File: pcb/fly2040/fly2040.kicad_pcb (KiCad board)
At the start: 4 copper layers, 23 x 18 mm, 47 parts, among them J1 Conn_01x02, J10 Conn_01x02, J2 Conn_01x02, J3 Conn_01x02, J4 Conn_01x02, J5 Conn_01x02, J6 Conn_01x02, J7 Conn_01x02, J8 Conn_01x06, J9 Conn_01x02, SW1 EVPAWED40, U1 RP2040, U2 W25Q16JVUXIQ, U3 RS0102YH8, U4 TPS613222ADBVR, X1 SMD-3225_4P_12.000MHZ_9PF

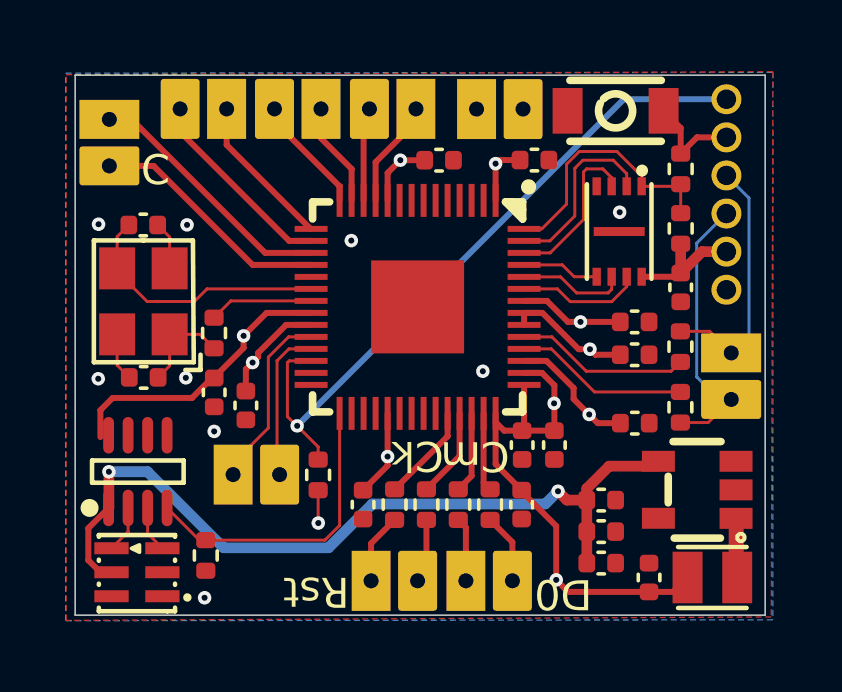
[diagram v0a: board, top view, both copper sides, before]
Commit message: Added more outputs. Improved board layout for panel. Added panel files
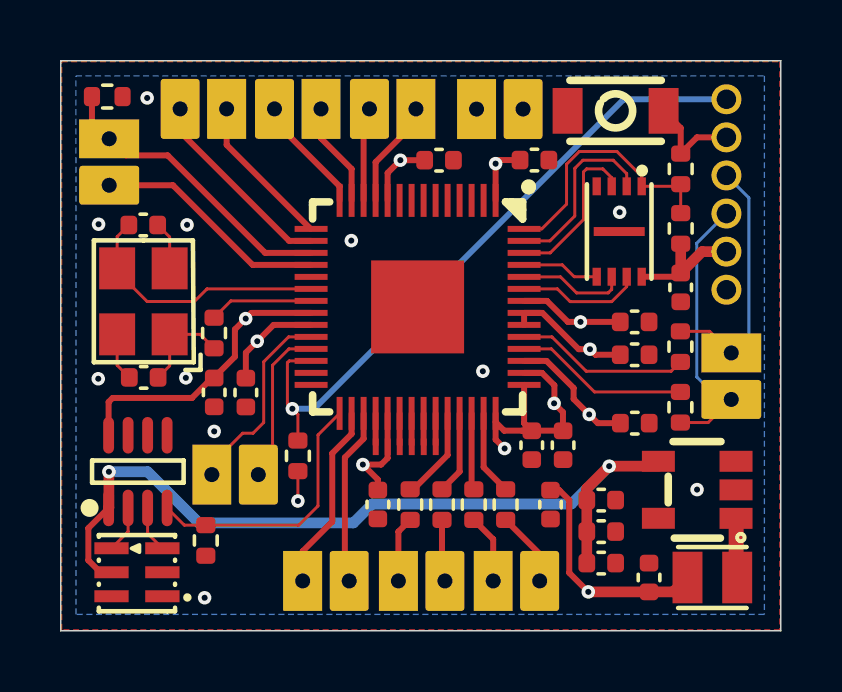
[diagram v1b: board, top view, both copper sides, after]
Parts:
- added J11: Conn_01x02, kicad_lceda:TH_Pads_1x02_P1.50mml, F.Cu at (78.5, 66.7)
- added J12: Conn_01x06, kicad_lceda:Pad_6Pin, F.Cu at (81.9, 64.1)
- added R12: 10k, Resistor_SMD:R_0402_1005Metric, F.Cu at (72.0, 50.6)
- moved C8 0.96 mm to (86.7, 64.2)
- moved R2 0.93 mm to (78.3, 62.6)
- moved J3 0.91 mm to (81.7, 66.7)
- moved J4 0.91 mm to (84.8, 66.7)
- moved J7 0.71 mm to (75.4, 63.2)
- moved J2 0.65 mm to (72.0, 52.0)
- moved R10 0.52 mm to (84.2, 64.2)
- moved R11 0.52 mm to (85.2, 64.2)
- moved R8 0.52 mm to (82.0, 64.2)
- moved R9 0.52 mm to (83.1, 64.2)
- moved R7 0.50 mm to (75.2, 65.4)
- moved C7 0.49 mm to (81.0, 64.2)
- moved C4 0.43 mm to (76.6, 60.5)
- moved C9 0.32 mm to (86.1, 62.2)
- moved C6 0.29 mm to (87.1, 62.2)
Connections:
- net NS_14 renamed NS_CPU_PD
- U1 pad 30: unconnected-(U1-GPIO19-Pad30) -> NS_19
- U1 pad 31: unconnected-(U1-GPIO20-Pad31) -> NS_20
- U1 pad 32: unconnected-(U1-GPIO21-Pad32) -> PAD_21
- U1 pad 34: unconnected-(U1-GPIO22-Pad34) -> PAD_22
- U1 pad 35: unconnected-(U1-GPIO23-Pad35) -> PAD_23
- U1 pad 36: unconnected-(U1-GPIO24-Pad36) -> PAD_24
- U1 pad 37: unconnected-(U1-GPIO25-Pad37) -> PAD_25
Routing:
- net NS_19: track 0.00 -> 6.26 mm
- net NS_20: track 0.00 -> 5.90 mm
- net NS_CPU_PD: track 7.82 -> 9.95 mm
- net LED_EN: track 10.1 -> 8.92 mm
- net PAD_25: track 0.00 -> 1.04 mm
- net PAD_24: track 0.00 -> 1.04 mm
- net PAD_23: track 0.00 -> 1.04 mm
- net PAD_22: track 0.00 -> 1.04 mm
- net PAD_21: track 0.00 -> 1.04 mm
- net +3V3: track 43.3 -> 42.3 mm, vias 8 -> 9
- net RST: track 23.3 -> 22.3 mm
- net DBG_CLK: track 5.73 -> 6.60 mm
- net +1V1: track 26.4 -> 25.7 mm
- net GND: vias 9 -> 11
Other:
- board size 23 x 18 mm -> 24 x 19 mm
- board text added: "19"
- board text added: "20"
- board text removed: "C"
- board text removed: "Ck"
- board text removed: "Cm"
- board text removed: "Rst"

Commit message: Added tiny double sided (ds) board.
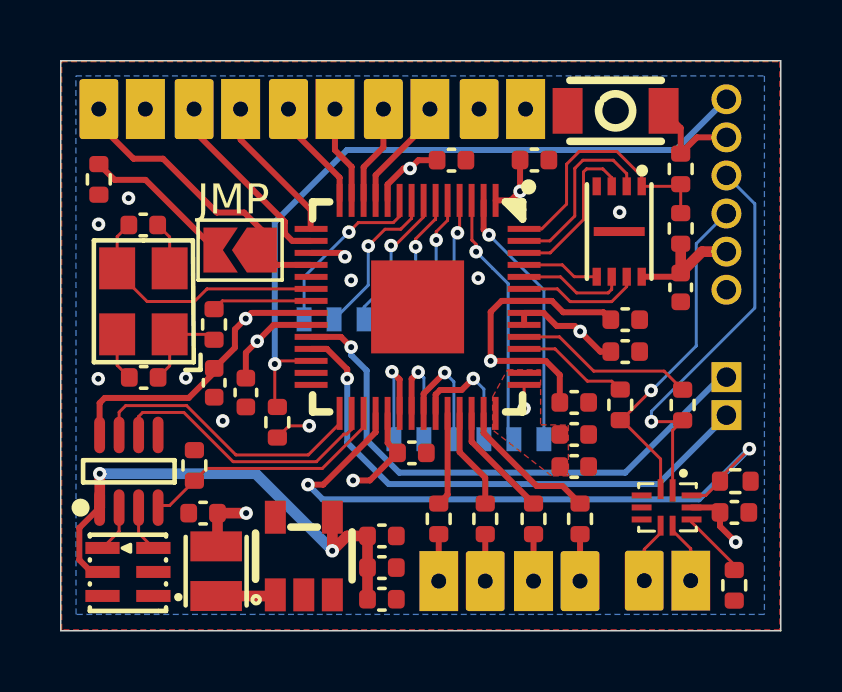
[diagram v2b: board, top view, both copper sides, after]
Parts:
- added JP1: Jumper_2_Open, kicad_lceda:SolderJumper-2_P1.3mm_Open_TrianglePad1.0x1.5mm_Sm, F.Cu at (76.4, 55.7)
- added R13: 10k, Resistor_SMD:R_0402_1005Metric, F.Cu at (92.9, 63.4)
- added R14: 10k, Resistor_SMD:R_0402_1005Metric, F.Cu at (92.8, 66.9)
- added U5: RS2227XUTQK10, kicad_lceda:WQFN-10_L1.8-W1.4-P0.40-BL, F.Cu at (90.6, 64.3)
- J11: value Conn_01x02 -> Conn_01x06; footprint kicad_lceda:TH_Pads_1x02_P1.50mml -> kicad_lceda:Pad_6Pin; moved to B.Cu
- J12: moved to B.Cu
- J7: footprint kicad_lceda:TH_Pads_1x02_P1.50mml -> kicad_lceda:PinHeader_Sm_1x02_P1.27mm_Vertical
- moved J7 17.5 mm to (92.6, 59.9), turned to 0 degrees
- moved L1 16.5 mm to (75.6, 66.4), turned to 90 degrees
- moved C15 15.0 mm to (75.1, 64.5), turned to 180 degrees
- moved U4 13.3 mm to (78.5, 65.9), turned to -90 degrees
- moved J5 7.71 mm to (91.4, 66.7), turned to -90 degrees
- moved C17 7.65 mm to (81.1, 67.3)
- moved C16 7.65 mm to (81.1, 66.3)
- moved C18 7.37 mm to (81.1, 65.2)
- moved J11 6.24 mm to (84.0, 63.9), turned to 180 degrees
- moved C8 6.14 mm to (92.9, 64.5), turned to 0 degrees
- moved J12 4.34 mm to (81.0, 59.9), turned to 180 degrees
- moved R12 2.77 mm to (71.7, 53.4), turned to -90 degrees
- moved R7 2.53 mm to (74.9, 62.9), turned to -90 degrees
- moved R11 2.53 mm to (87.7, 64.7)
- moved C5 2.13 mm to (87.5, 60.8)
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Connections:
- J11 pad 1: NS_19 -> NS_0
- J11 pad 2: NS_20 -> NS_1
- J12 pad 1: PAD_21 -> NS_2
- J12 pad 2: +3V3 -> NS_3
- J12 pad 3: PAD_22 -> NS_4
- J12 pad 4: PAD_23 -> NS_5
- J12 pad 5: PAD_24 -> NS_6
- J12 pad 6: PAD_25 -> NS_7
- J2 pad 1: NS_CPU_PD -> NS_14
- J5 pad 1: D+ -> D+_CXN
- J5 pad 2: D- -> D-_CXN
- R12 pad 1: NS_CPU_PD -> Net-(JP1-B)
- U1 pad 17: NS_CPU_PD -> NS_14
- U1 pad 2: unconnected-(U1-GPIO0-Pad2) -> NS_0
- U1 pad 29: LED_EN -> LED_CLK
- U1 pad 3: unconnected-(U1-GPIO1-Pad3) -> NS_1
- U1 pad 30: NS_19 -> LED_DATA
- U1 pad 31: NS_20 -> LED_EN
- U1 pad 32: PAD_21 -> USB_SEL
- U1 pad 4: unconnected-(U1-GPIO2-Pad4) -> NS_2
- U1 pad 5: unconnected-(U1-GPIO3-Pad5) -> NS_3
- U1 pad 6: unconnected-(U1-GPIO4-Pad6) -> NS_4
- U1 pad 7: unconnected-(U1-GPIO5-Pad7) -> NS_5
- U1 pad 8: unconnected-(U1-GPIO6-Pad8) -> NS_6
- U1 pad 9: unconnected-(U1-GPIO7-Pad9) -> NS_7
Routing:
- net USB_SEL: track 0.00 -> 21.9 mm, vias 0 -> 2
- net DBG_DAT: track 5.35 -> 18.1 mm, vias 0 -> 1
- net DBG_CLK: track 6.60 -> 18.5 mm, vias 0 -> 1
- net +3V3: track 42.3 -> 31.7 mm
- net NS_14: track 0.00 -> 10.1 mm, vias 0 -> 1
- net +5V: track 27.2 -> 17.2 mm
- net NS_CPU_PD: track 9.95 -> 0.00 mm
- net LED_CLK: track 0.00 -> 9.65 mm
- net LED_DATA: track 0.00 -> 9.43 mm
- net NS_0: track 0.00 -> 8.79 mm, vias 0 -> 1
- net NS_1: track 0.00 -> 8.55 mm, vias 0 -> 1
- net NS_19: track 6.26 -> 0.00 mm
- net NS_7: track 0.00 -> 5.97 mm, vias 0 -> 1
- net NS_20: track 5.90 -> 0.00 mm
- net D+: track 7.63 -> 13.4 mm, vias 0 -> 1
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- added copper zone on F.Cu, net +3V3
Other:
- board text added: "+"
- board text added: "-"
- board text added: "14"
- board text added: "3V3"
- board text added: "B"
- board text added: "G"
- board text added: "JMP"
- board text added: "R"
- board text removed: "19"
- board text removed: "20"

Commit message: Updated main board with bus isolation ICs
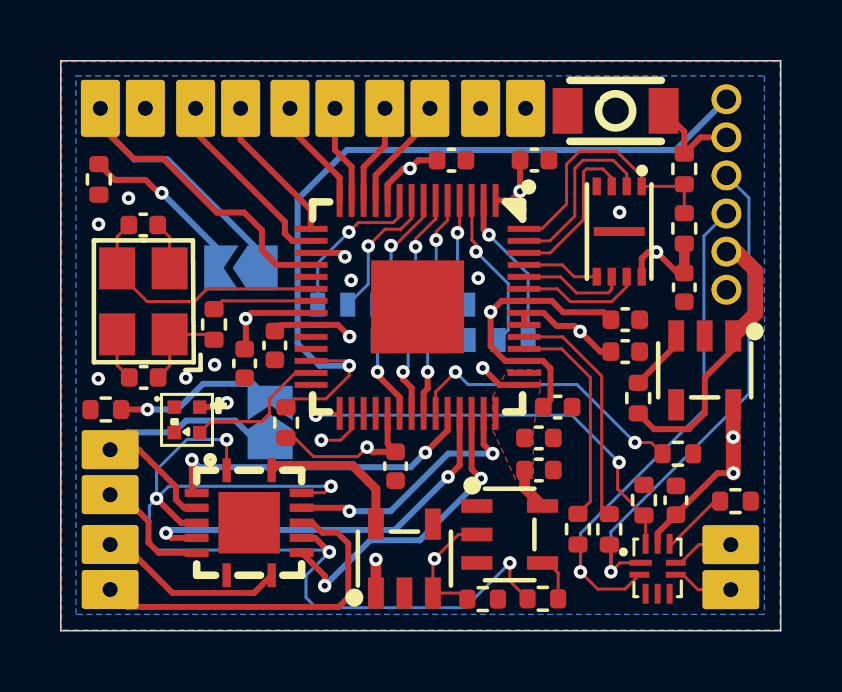
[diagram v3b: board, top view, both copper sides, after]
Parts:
- removed C15: 4.7uF,10V,X5R, Capacitor_SMD:C_0402_1005Metric
- removed C16, C17: 10uF,6.3V,X5R, Capacitor_SMD:C_0402_1005Metric
- removed C18: 2.2uF,6.3V,X5R, Capacitor_SMD:C_0402_1005Metric
- removed J7: Conn_01x02, kicad_lceda:PinHeader_Sm_1x02_P1.27mm_Vertical
- removed L1: SPS20162R2MPCA, kicad_lceda:IND-SMD_L2.0-W1.6
- removed LED1: SK9822-EC20, kicad_lceda:LED-SMD_6P-L2.0-W2.0-P0.80-TL
- removed R10, R11: 47, Resistor_SMD:R_0402_1005Metric
- added JP2: Jumper_2_Open, kicad_lceda:SolderJumper-2_P1.3mm_Open_TrianglePad1.0x1.5mm_Sm, B.Cu at (77.4, 61.5)
- added R15: 10k, Resistor_SMD:R_0402_1005Metric, F.Cu at (84.5, 67.3)
- added R16: 10k, Resistor_SMD:R_0402_1005Metric, F.Cu at (86.5, 67.3)
- added U6: SN74CBTLV3125RGYR, kicad_lceda:VQFN-14_L3.5-W3.5-P0.50-BL-EP, F.Cu at (76.7, 64.8)
- added U7: XL-1010RGBC-WS2812B, kicad_lceda:LED-SMD_4P-L1.0-W1.0-TL_XL-1010RGBC-WS2812B, F.Cu at (74.6, 61.4)
- added U8: 74LVC1GU04GV,125, kicad_lceda:SC-74A-5_L2.9-W1.6-P0.95-LS2.8-BL, F.Cu at (85.4, 65.2)
- JP1: moved to B.Cu
- R7: value 10K -> 10k
- R8, R9: value 47 -> 10k
- U3: value RS0102YH8 -> RT9078-25GJ5; footprint kicad_lceda:SOT-23-8_L3.0-W1.7-P0.65-LS2.8-BL -> kicad_lceda:TSOT-23-5_L2.9-W1.6-P0.95-LS2.8-BL
- U4: value TPS613222ADBVR -> RT9080-33GJ5; footprint kicad_lceda:TSOT-23-5_L2.9-W1.6-P0.95-LS2.8-BR -> kicad_lceda:TSOT-23-5_L2.9-W1.6-P0.95-LS2.8-BL
- moved R7 16.1 mm to (91.0, 62.5), turned to 0 degrees
- moved U4 14.7 mm to (91.9, 59.7), turned to 180 degrees
- moved J4 14.2 mm to (72.0, 65.5), turned to 0 degrees
- moved R9 13.2 mm to (71.9, 61.0), turned to 180 degrees
- moved J3 11.8 mm to (72.0, 62.4), turned to 0 degrees
- moved U3 9.63 mm to (81.9, 66.0)
- moved R8 7.77 mm to (89.7, 60.6), turned to 90 degrees
- moved R3 4.81 mm to (88.7, 65.0)
- moved R4 4.38 mm to (87.6, 65.0)
- moved J11 3.35 mm to (83.5, 60.6)
- moved R13 3.11 mm to (89.8, 64.0), turned to -90 degrees
- moved R14 2.81 mm to (92.9, 64.1), turned to 0 degrees
- moved U5 2.07 mm to (90.3, 66.3), turned to -90 degrees
- moved C8 1.99 mm to (90.9, 64.0), turned to 90 degrees
- moved C4 1.84 mm to (77.5, 58.9)
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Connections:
- J11 pad 3: PAD_25 -> GND
- J3 pad 1: NS_RST -> NS_RST_OUT
- J3 pad 2: NS_CLK -> NS_CLK_OUT
- J4 pad 1: NS_CMD -> NS_CMD_OUT
- J4 pad 2: NS_D0 -> NS_D0_OUT
- J8 pad 5: +3V3 -> +5V
- R7 pad 1: GND -> BOARD_DET
- R7 pad 2: LED_EN -> GND
- R8 pad 1: Net-(U1-GPIO26_ADC0) -> +5V
- R8 pad 2: NS_RST -> Net-(U4-EN)
- R9 pad 1: Net-(U1-GPIO27_ADC1) -> Net-(JP2-B)
- R9 pad 2: NS_CLK -> GND
- U1 pad 27: unconnected-(U1-GPIO16-Pad27) -> LED_DATA
- U1 pad 28: unconnected-(U1-GPIO17-Pad28) -> PAD_17
- U1 pad 29: LED_CLK -> USB_SEL
- U1 pad 30: LED_DATA -> MMC_SEL
- U1 pad 31: LED_EN -> PAD_20
- U1 pad 32: USB_SEL -> PAD_21
- U1 pad 37: PAD_25 -> BOARD_DET
- U1 pad 38: Net-(U1-GPIO26_ADC0) -> NS_RST
- U1 pad 39: Net-(U1-GPIO27_ADC1) -> NS_CLK
- U1 pad 40: Net-(U1-GPIO28_ADC2) -> NS_CMD
- U1 pad 41: Net-(U1-GPIO29_ADC3) -> NS_D0
- U3 pad 1: +5V -> +3V3
- U3 pad 2: LED_CLK_5V -> GND
- U3 pad 3: LED_DATA_5V -> MMC_SEL
- U3 pad 4: LED_EN -> unconnected-(U3-SNS/NC-Pad4)
- U3 pad 5: GND -> +2V5
- U4 pad 1: Net-(U4-SW) -> +5V
- U4 pad 3: unconnected-(U4-NC-Pad3) -> Net-(U4-EN)
- U4 pad 4: +5V -> unconnected-(U4-NC-Pad4)
- U4 pad 5: unconnected-(U4-NC-Pad5) -> +3V3
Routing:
- net MMC_SEL_INV: track 0.00 -> 33.1 mm, vias 0 -> 5
- net DBG_CLK: track 18.5 -> 0.00 mm, vias 1 -> 0
- net DBG_DAT: track 18.1 -> 0.00 mm, vias 1 -> 0
- net NS_CLK: track 1.56 -> 13.5 mm, vias 0 -> 2
- net NS_D0_OUT: track 0.00 -> 11.9 mm
- net MMC_SEL: track 0.00 -> 11.4 mm, vias 0 -> 2
- net NS_RST_OUT: track 0.00 -> 10.0 mm
- net BOARD_DET: track 0.00 -> 9.68 mm, vias 0 -> 2
- net LED_CLK: track 9.65 -> 0.00 mm
- net NS_RST: track 1.56 -> 10.9 mm, vias 0 -> 2
- net NS_CMD: track 1.56 -> 10.4 mm, vias 0 -> 2
- net LED_EN: track 8.42 -> 0.00 mm
- net NS_CPU: track 9.91 -> 18.1 mm
- net +5V: track 17.2 -> 9.35 mm, vias 2 -> 0
- net USB_SEL: track 21.9 -> 14.7 mm
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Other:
- board text added: "5V"
- board text removed: "3V3"
- board text removed: "DC"
- board text removed: "DD"
- board text removed: "JMP"
